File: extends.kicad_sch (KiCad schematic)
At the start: 29 parts, among them J15 Conn_02x04_Odd_Even, J5 PORT-A-0-15, J6 Conn_02x22_Odd_Even, J7 Conn_02x22_Odd_Even, J9 PORT-C-B-0-15, SW3 WAKEUP0

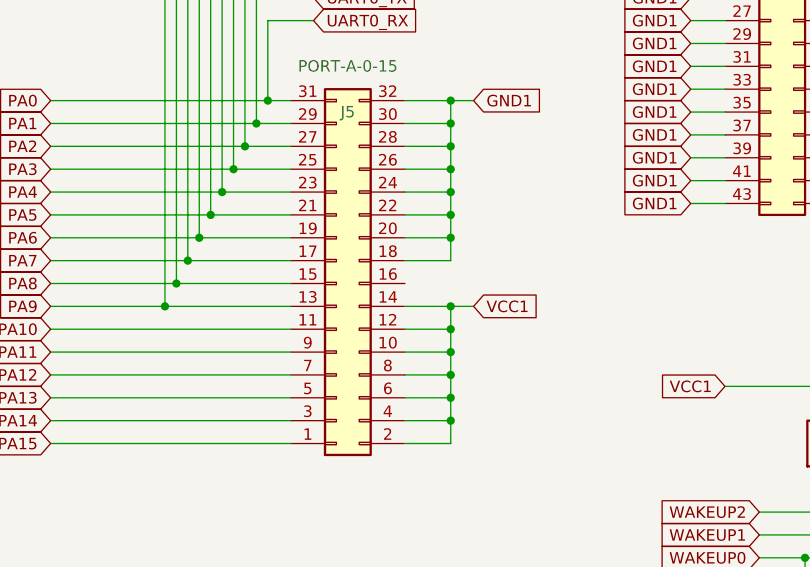
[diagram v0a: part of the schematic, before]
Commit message: Питание 5V от JTAG, множественные исправления
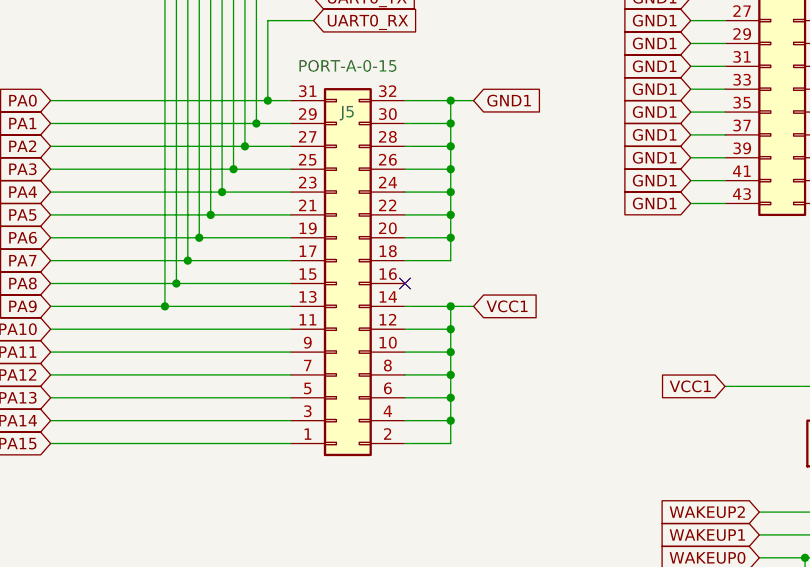
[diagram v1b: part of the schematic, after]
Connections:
- no-connect marks 0 -> 1
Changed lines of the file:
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@@
 		(color 0 0 0 0)
+	)
+	(no_connect
+		(at 166.37 88.9)
 	)
 	(wire
